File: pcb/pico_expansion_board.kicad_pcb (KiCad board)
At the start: 4 copper layers, 91.7 x 66.8 mm, 57 parts, among them IC1 TPS5450DDA, J1 DC12V/24V, J2 TMC2209 Motor 1, J3 TMC2209 Motor 2, J4 Motor 1, J5 Motor 2, J8 EXP1, J9 EXP2, SW1 SW_Push, U1 MAX3232, U2 Pico, U3 CAT24C256, U4 74LVC1G125, U5 AMS1117-3.3

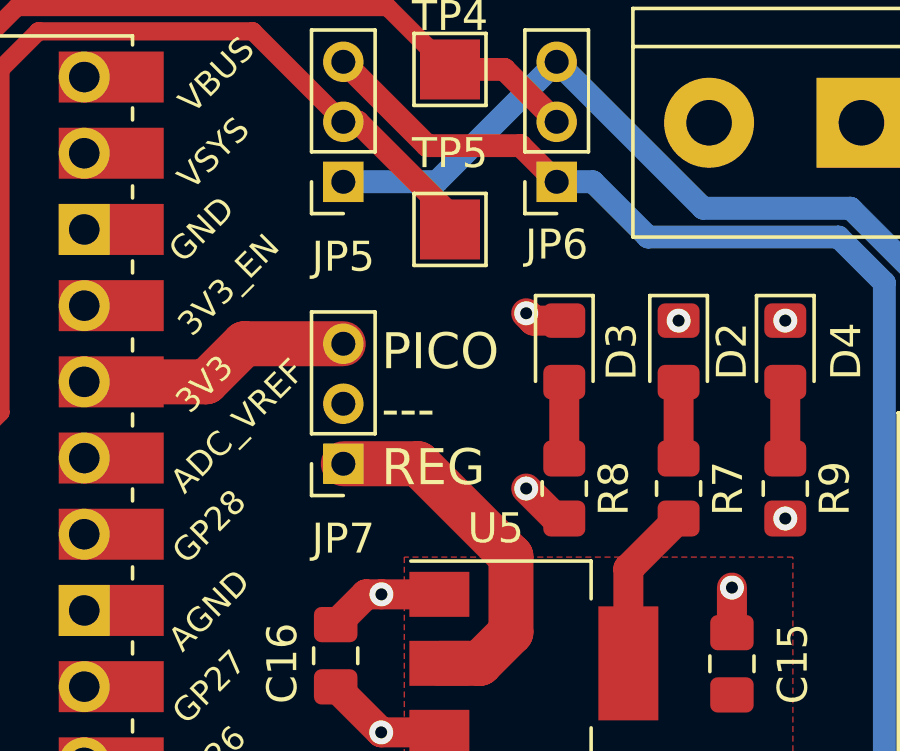
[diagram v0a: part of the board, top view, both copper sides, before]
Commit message: Update 3D model mapping, fix the footprint for jumpers
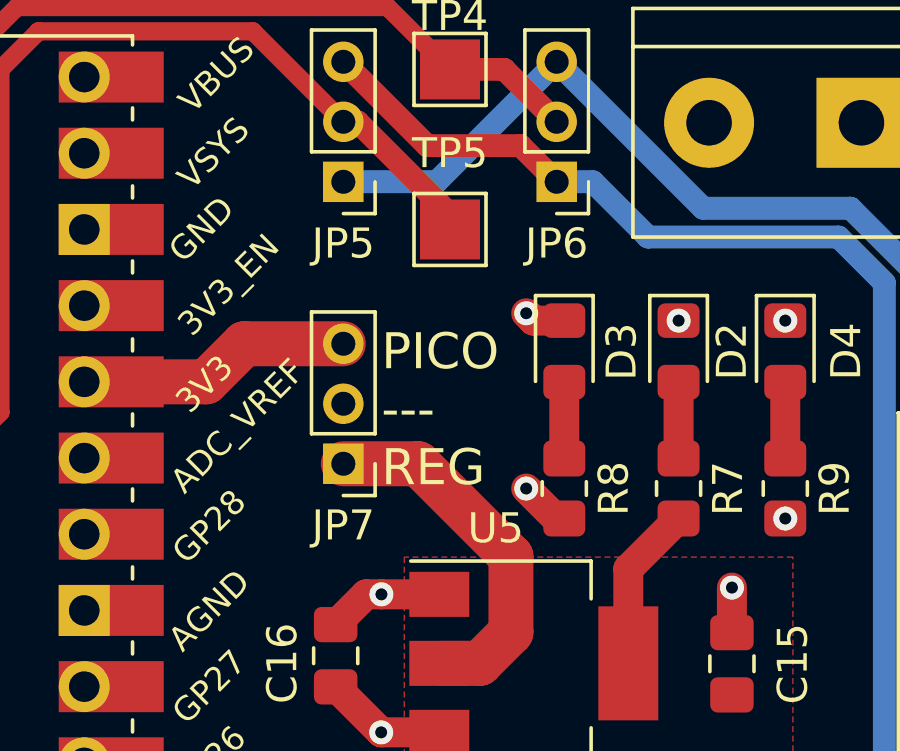
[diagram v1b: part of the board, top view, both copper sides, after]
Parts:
- JP5, JP6, JP7: footprint Connector_PinSocket_2.00mm:PinSocket_1x03_P2.00mm_Vertical -> Connector_PinHeader_2.00mm:PinHeader_1x03_P2.00mm_Vertical

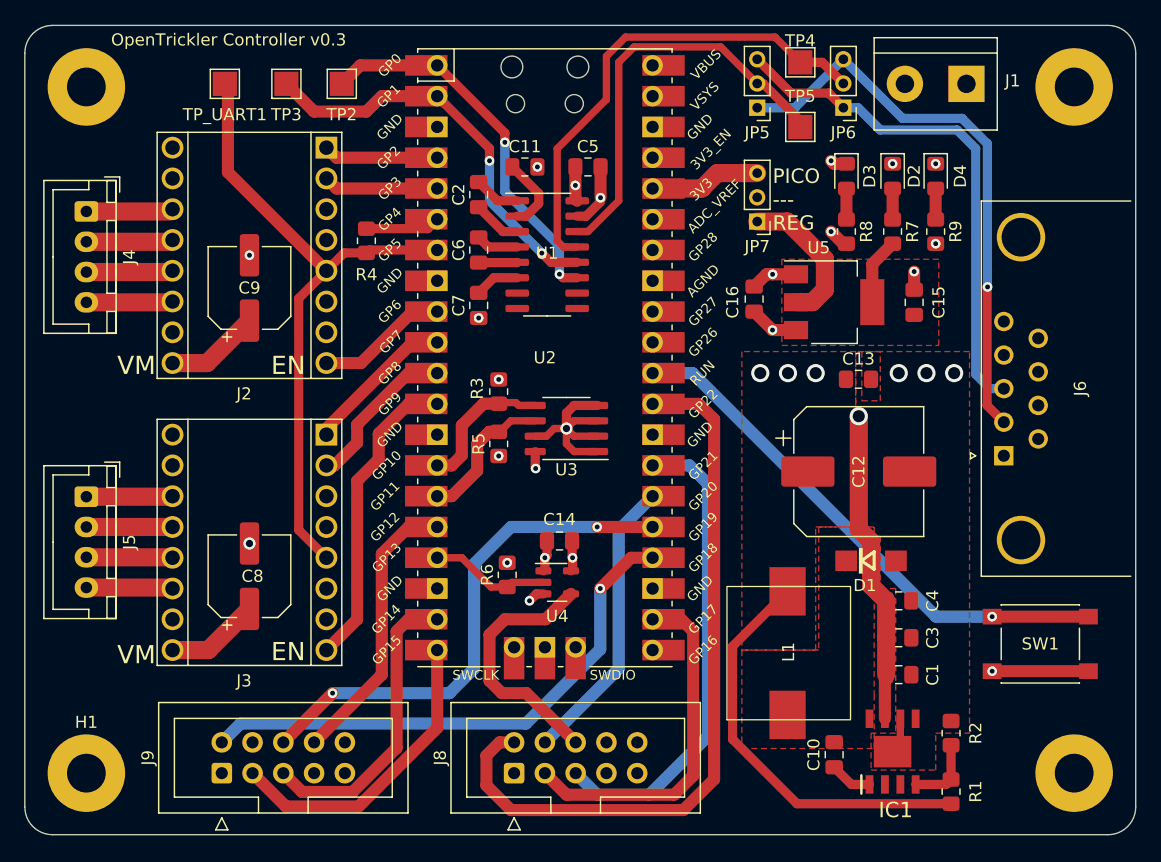
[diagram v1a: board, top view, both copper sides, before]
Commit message: Fix the bug where Pin 5 from RS232 was not connected to the ground, update several labels
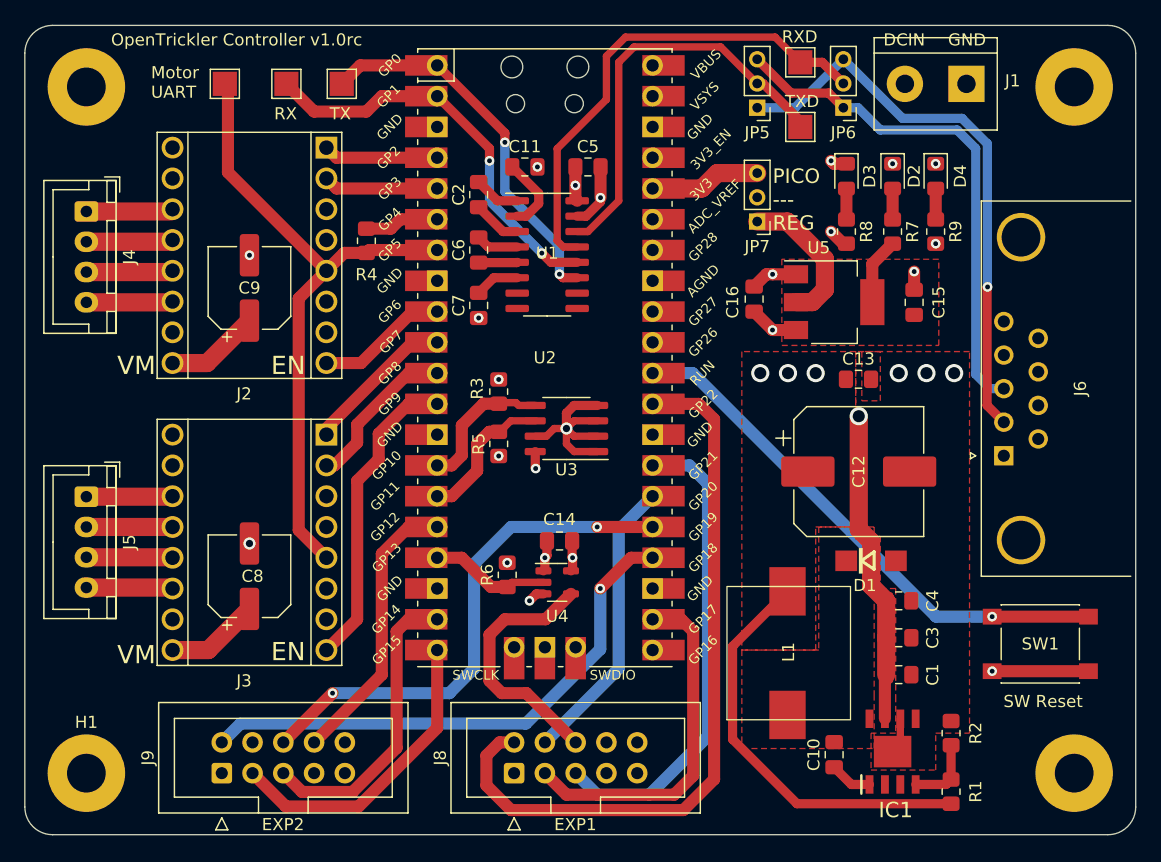
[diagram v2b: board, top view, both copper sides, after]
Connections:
- H1 pad 1: (no net) -> GND
- H2 pad 1: (no net) -> GND
- H3 pad 1: (no net) -> GND
- H4 pad 1: (no net) -> GND
- J6 pad 5: unconnected-(J6-Pad5) -> GND
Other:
- board text added: "DCIN"
- board text added: "GND"
- board text added: "Motor UART"
- board text added: "OpenTrickler Controller v1.0rc"
- board text added: "RX"
- board text added: "RXD"
- board text added: "SW Reset"
- board text added: "TX"
- board text added: "TXD"
- board text removed: "OpenTrickler Controller v0.3"

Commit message: Update silkscreen
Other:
- board text added: "3.3V"
- board text added: "5V"
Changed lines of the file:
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@@
     (property "ki_keywords" "LED diode")
     (attr smd)
-    (fp_text reference "D2" (at 0 -1.778 90) (layer "F.SilkS")
+    (fp_text reference "D2" (at -1.016 -1.778 90) (layer "F.SilkS")
         (effects (font (size 1 1) (thickness 0.15)))
     )
@@
     (property "ki_keywords" "LED diode")
     (attr smd)
-    (fp_text reference "D4" (at 0 -2.032 90) (layer "F.SilkS")
+    (fp_text reference "D4" (at -1.016 -2.032 90) (layer "F.SilkS")
         (effects (font (size 1 1) (thickness 0.15)))
     )
@@
     (property "ki_keywords" "LED diode")
     (attr smd)
-    (fp_text reference "D3" (at 0.009 -1.913 90) (layer "F.SilkS")
+    (fp_text reference "D3" (at -1.016 -1.913 90) (layer "F.SilkS")
         (effects (font (size 1 1) (thickness 0.15)))
     )
@@
     (effects (font (size 1 1) (thickness 0.1875)) (justify left bottom))
   )
+  (gr_text "3.3V" (at 144.018 89.662 90) (layer "F.SilkS")
+    (effects (font (size 0.8 0.8) (thickness 0.1)) (justify left bottom))
+  )
+  (gr_text "5V" (at 140.208 89.408 90) (layer "F.SilkS")
+    (effects (font (size 0.8 0.8) (thickness 0.1)) (justify left bottom))
+  )
   (gr_text "OpenTrickler Controller v1.0rc" (at 77.216 75.946) (layer "F.SilkS")
     (effects (font (size 1 1) (thickness 0.1875)) (justify left bottom))
@@
     (effects (font (size 1 1) (thickness 0.125)) (justify left bottom))
   )
+  (gr_text "DCIN" (at 147.574 89.916 90) (layer "F.SilkS")
+    (effects (font (size 0.8 0.8) (thickness 0.1)) (justify left bottom))
+  )
   (gr_text "VM" (at 77.724 103.124) (layer "F.SilkS")
